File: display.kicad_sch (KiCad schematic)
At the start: 72 parts, among them IC11 SN74LV1T125DBVR, IC6 PCA9517ADP, J1 46756-1001, J2 2129320-3, T1 BSS138APW

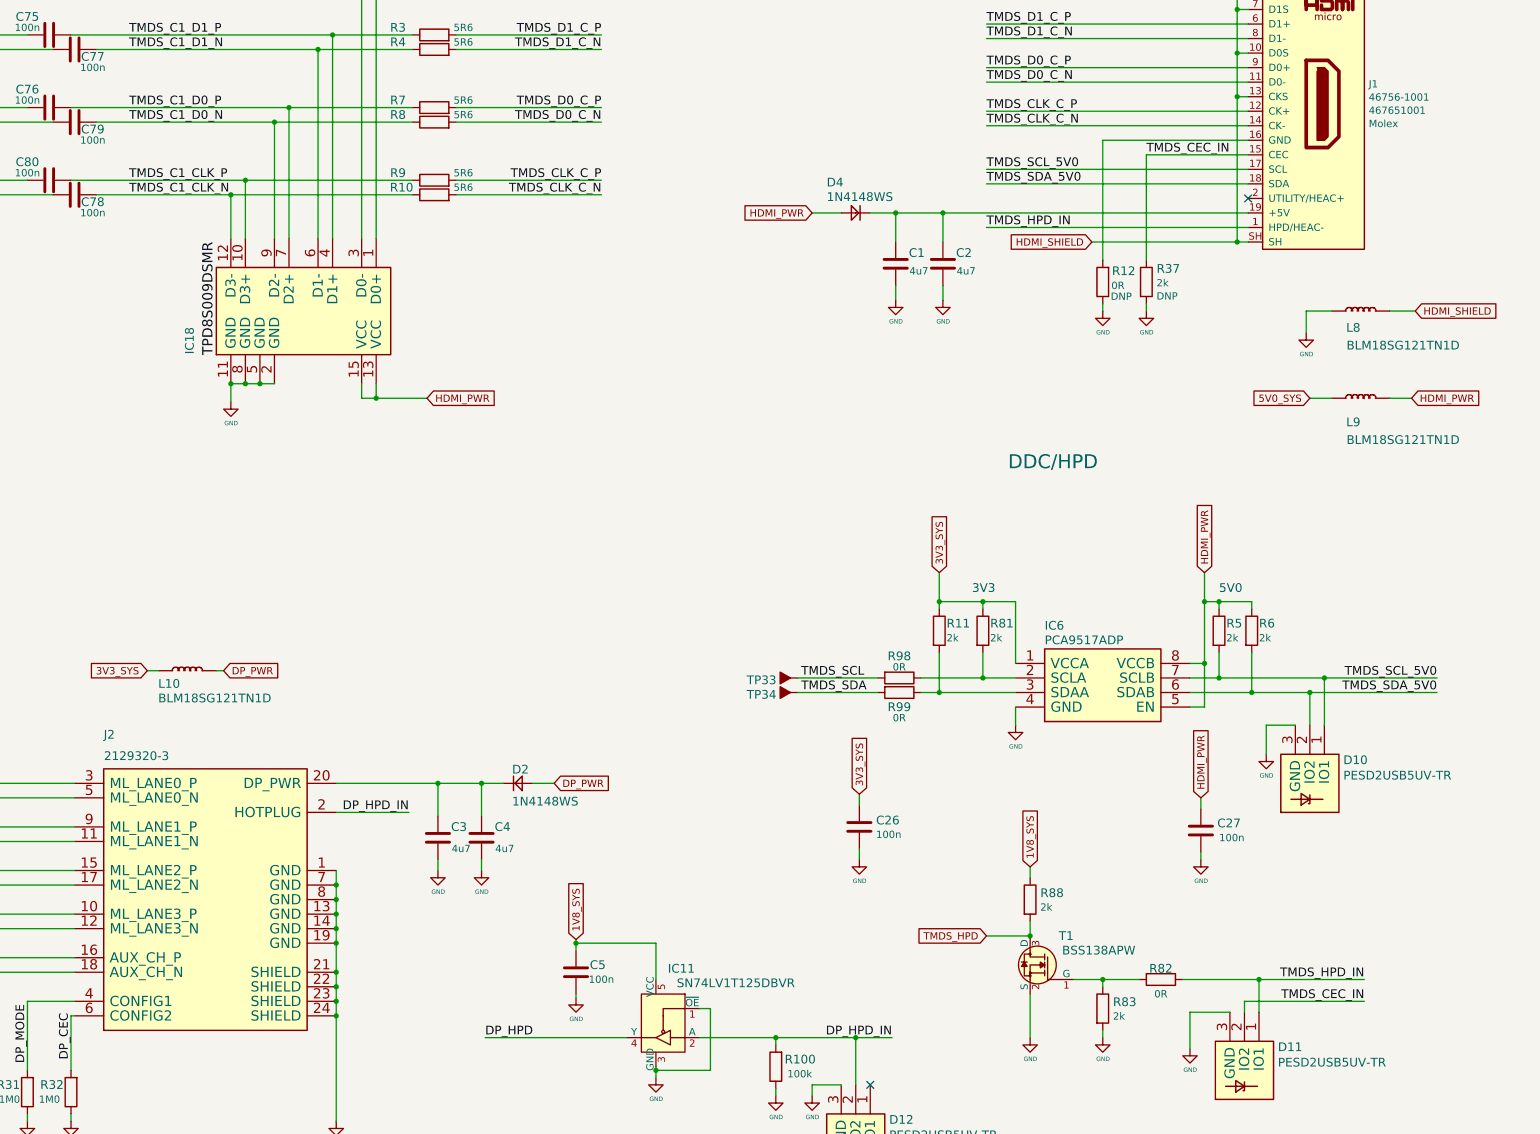
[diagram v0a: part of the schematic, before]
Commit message: WIP: Re-design base board
1. change to more common connector from JLC
2. add WIFI M.2 Key-E connector
3. add USB Hub which contained in nVidia version board
4. change DC connecotor to XT30
5. change USB Mico-B to USB Type C
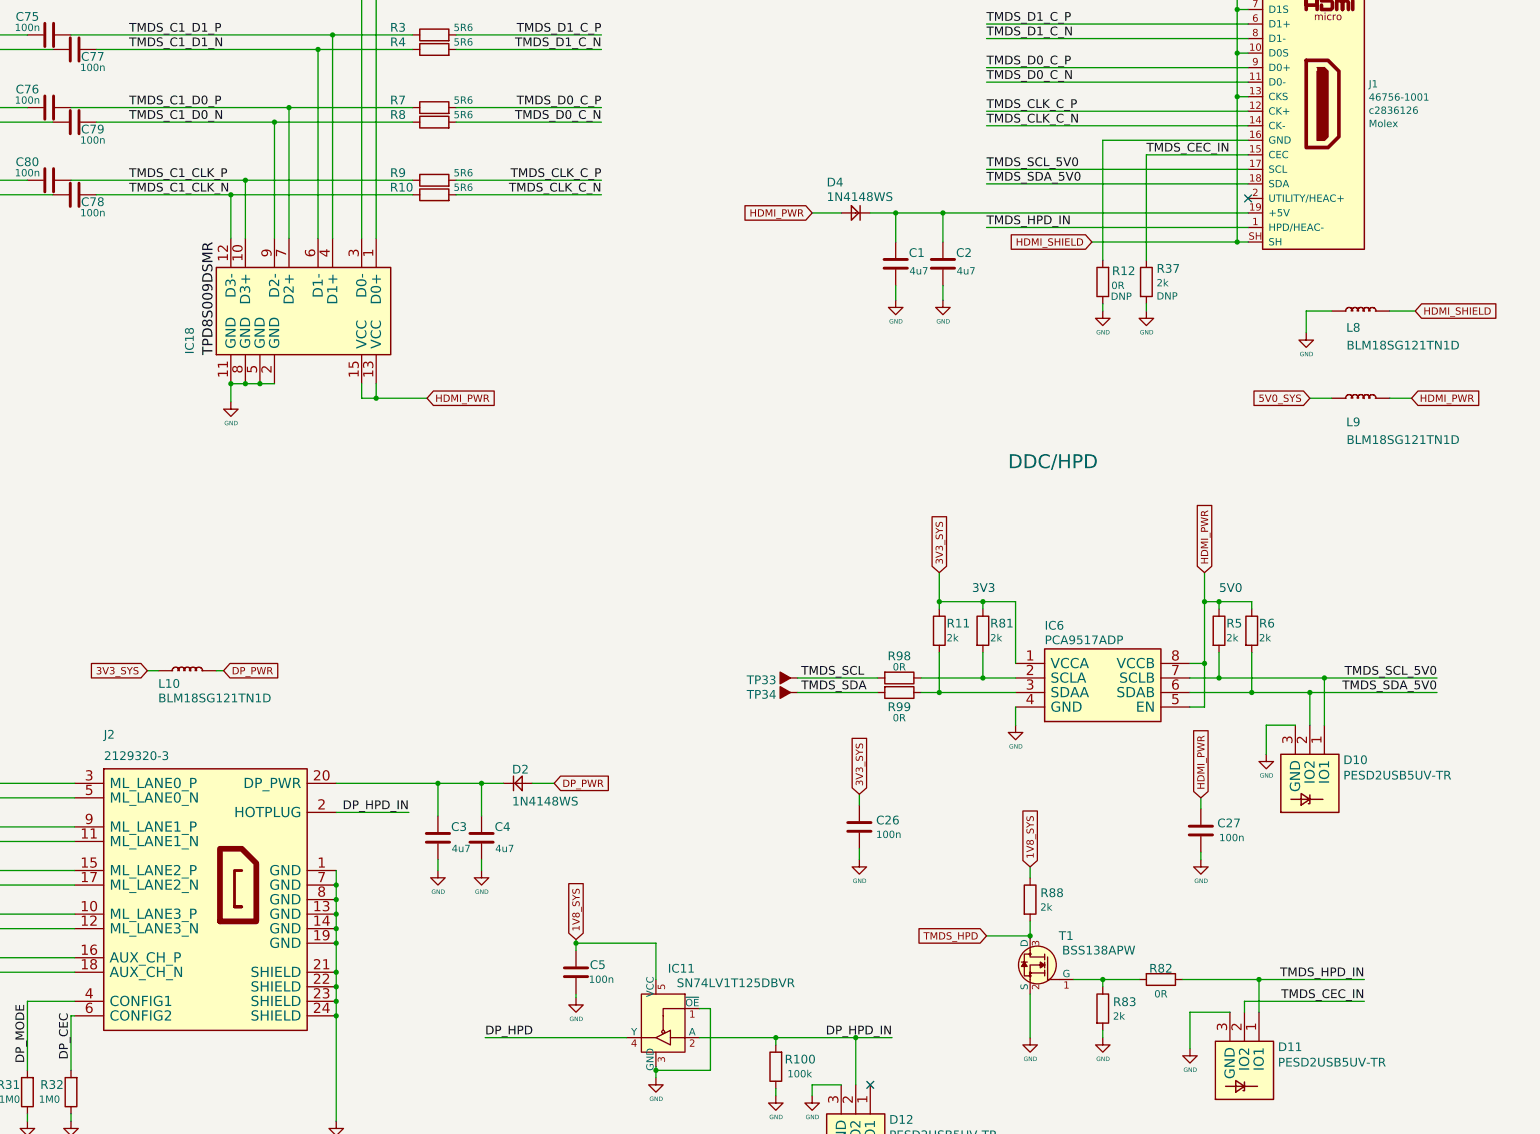
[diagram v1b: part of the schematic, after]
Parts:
- J1: footprint jetson-nano-baseboard-footprints:HDMI_Micro-D_Molex_46765-1x01 -> JLC_Footprint:HDMI-SMD_HDMI-001C; MPN 467651001 -> c2836126
- J2: footprint jetson-nano-baseboard-footprints:2129320-3 -> JLC_Footprint:DP-SMD_HYC16-DP20-178
